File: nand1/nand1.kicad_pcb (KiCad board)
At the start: 2 copper layers, 14 parts, among them J1 JACK-DC, J2 JACK-MONO, U1 4093

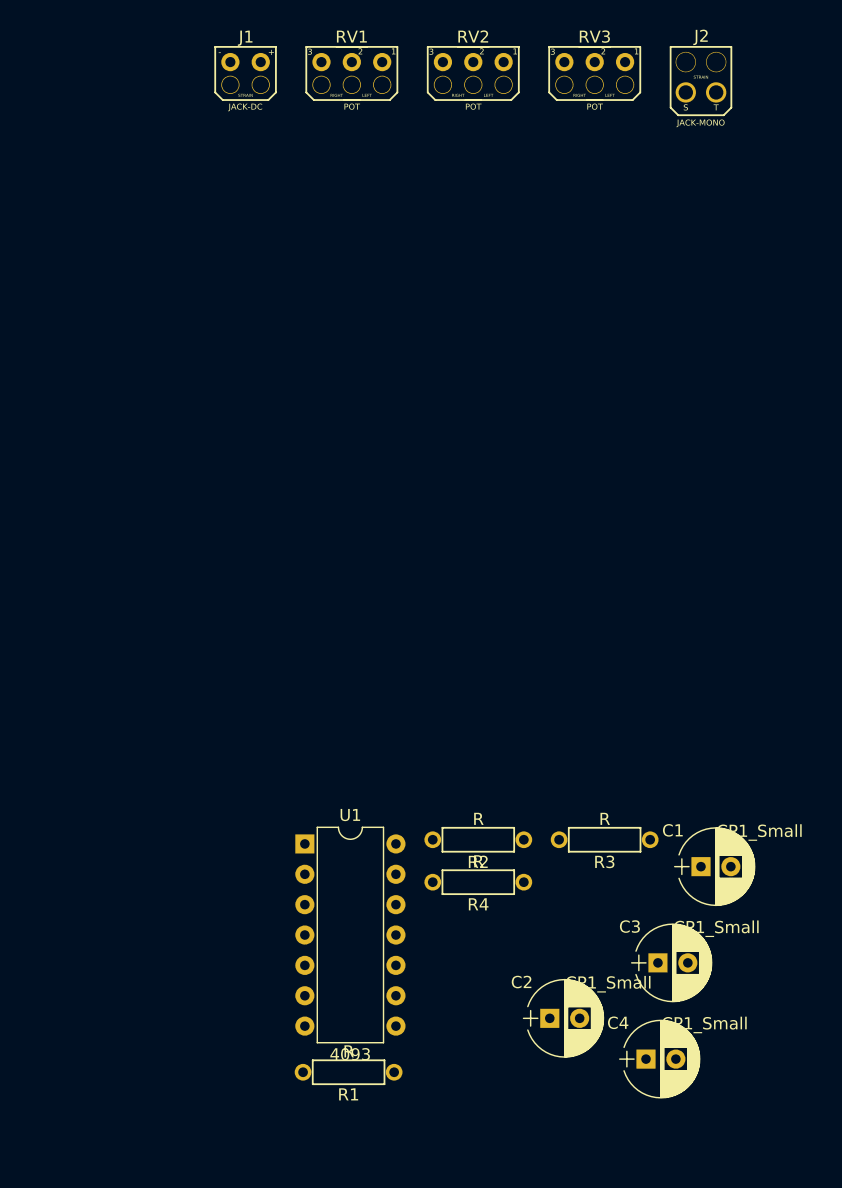
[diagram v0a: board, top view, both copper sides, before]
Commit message: Made pcblayout for etching
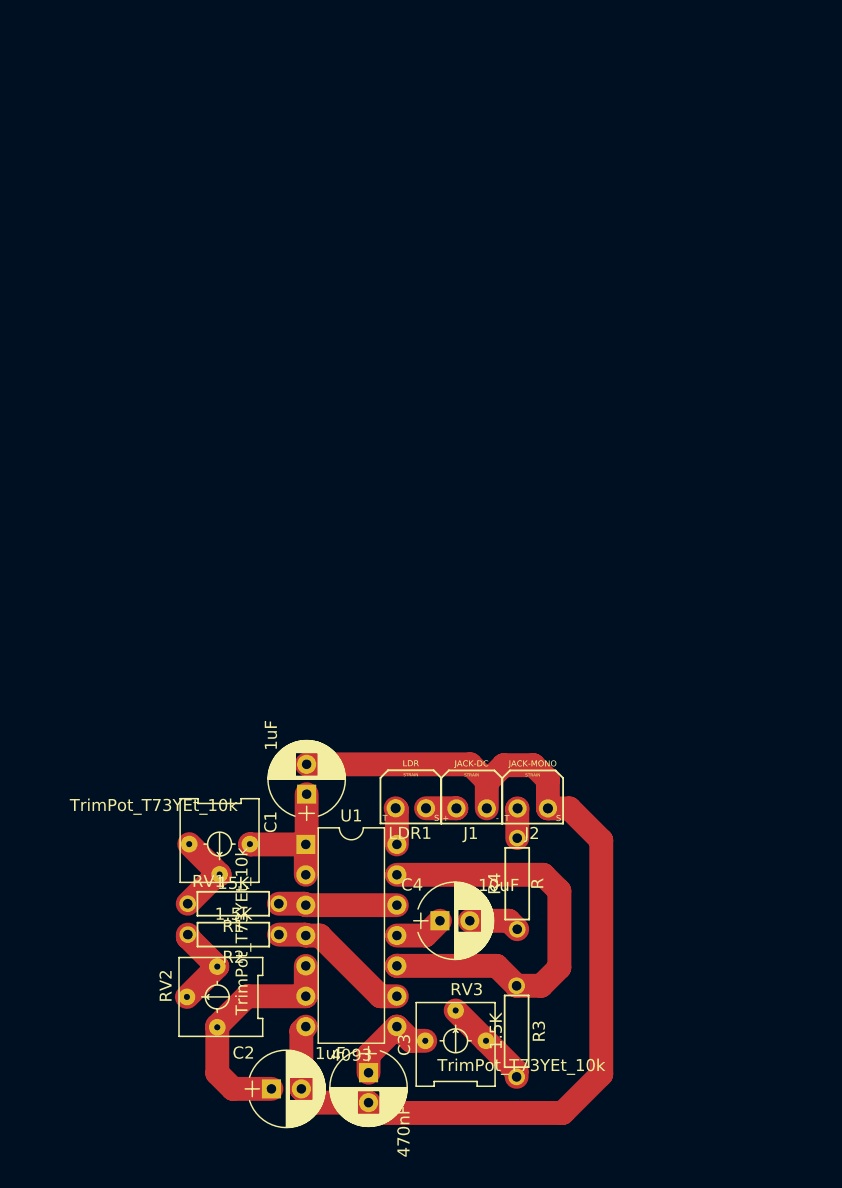
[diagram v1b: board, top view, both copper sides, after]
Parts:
- added LDR1: LDR, Z-FP:Jack_Instrument, F.Cu at (118.0, 104.3)
- C1, C2: value CP1_Small -> 1uF
- C3: value CP1_Small -> 470nF
- C4: value CP1_Small -> 10uF
- J1: footprint zfoot:Jack_DC -> Z-FP:Jack_DC
- J2: footprint zfoot:Jack_Instrument_Bigger -> Z-FP:Jack_Instrument
- R1: value R -> 15K
- R2, R3: value R -> 1.5K
- RV1, RV2, RV3: value POT -> TrimPot_T73YEt_10k; footprint zfoot:Pot_Wired -> 4ms_Potentiometer:Pot_Trim_7x6.6mm_T73YE
- moved RV3 82.7 mm to (121.7, 123.8), turned to 0 degrees
- moved RV2 81.1 mm to (101.8, 120.1), turned to 90 degrees
- moved RV1 66.4 mm to (102.0, 107.3)
- moved J1 65.2 mm to (123.0, 104.3), turned to 0 degrees
- moved J2 62.8 mm to (128.2, 104.3)
- moved C1 33.5 mm to (109.2, 103.2), turned to 90 degrees
- moved C3 25.9 mm to (114.4, 126.5), turned to 270 degrees
- moved C2 24.0 mm to (106.3, 127.8)
- moved R2 22.0 mm to (103.1, 114.9)
- moved C4 20.8 mm to (120.4, 113.7)
- moved R3 17.6 mm to (126.8, 123.0), turned to 90 degrees
- moved R1 17.1 mm to (103.1, 112.3)
- moved R4 3.26 mm to (126.9, 110.6), turned to 270 degrees
- moved U1 0.09 mm to (109.2, 107.4)
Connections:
- J1 pad 1: +9V -> Net-(J1-Pad1)
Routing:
- net GND: track 0.00 -> 84.3 mm
- net Net-(R3-Pad2): track 0.00 -> 35.5 mm
- net Net-(C2-Pad1): track 0.00 -> 20.0 mm
- net Net-(R2-Pad2): track 0.00 -> 12.0 mm
- net Net-(C1-Pad1): track 0.00 -> 11.5 mm
- net Net-(R1-Pad2): track 0.00 -> 9.93 mm
- net Net-(C3-Pad1): track 0.00 -> 7.71 mm
- net Net-(R3-Pad1): track 0.00 -> 7.67 mm
- net Net-(R2-Pad1): track 0.00 -> 7.29 mm
- net Net-(R1-Pad1): track 0.00 -> 7.27 mm
- net Net-(C4-Pad2): track 0.00 -> 4.26 mm
- net Net-(C4-Pad1): track 0.00 -> 4.11 mm
- net +9V: track 0.00 -> 3.07 mm
- net Net-(J1-Pad1): track 0.00 -> 2.55 mm
- net Net-(J2-Pad1): track 0.00 -> 2.50 mm
